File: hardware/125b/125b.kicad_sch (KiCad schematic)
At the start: 56 parts, among them J1 Guitar in, J2 fsw pin 1, J3 fsw pin 2, J4 fsw pin 4, J5 fsw pin 5, J6 fsw pin 6, J7 Left out, J8 Right out, J9 fsw pin 3, SW1 Switch 1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

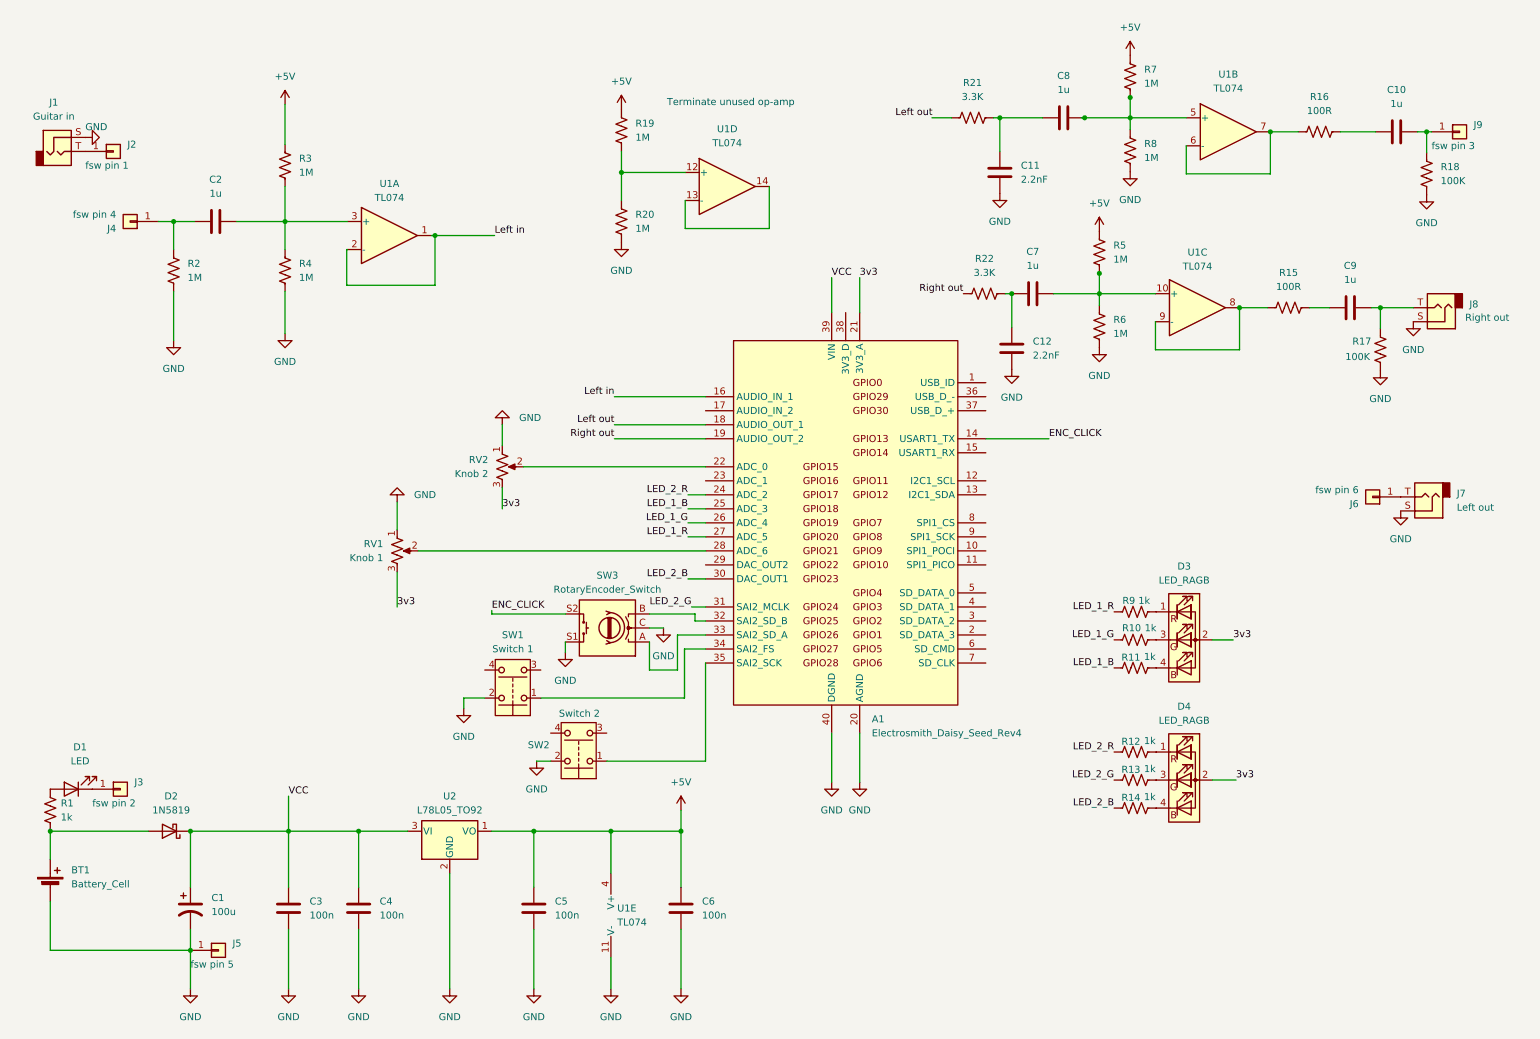
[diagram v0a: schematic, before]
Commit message: Add switch for line input toggle and fix stereo out
Bypass will be different for stereo out
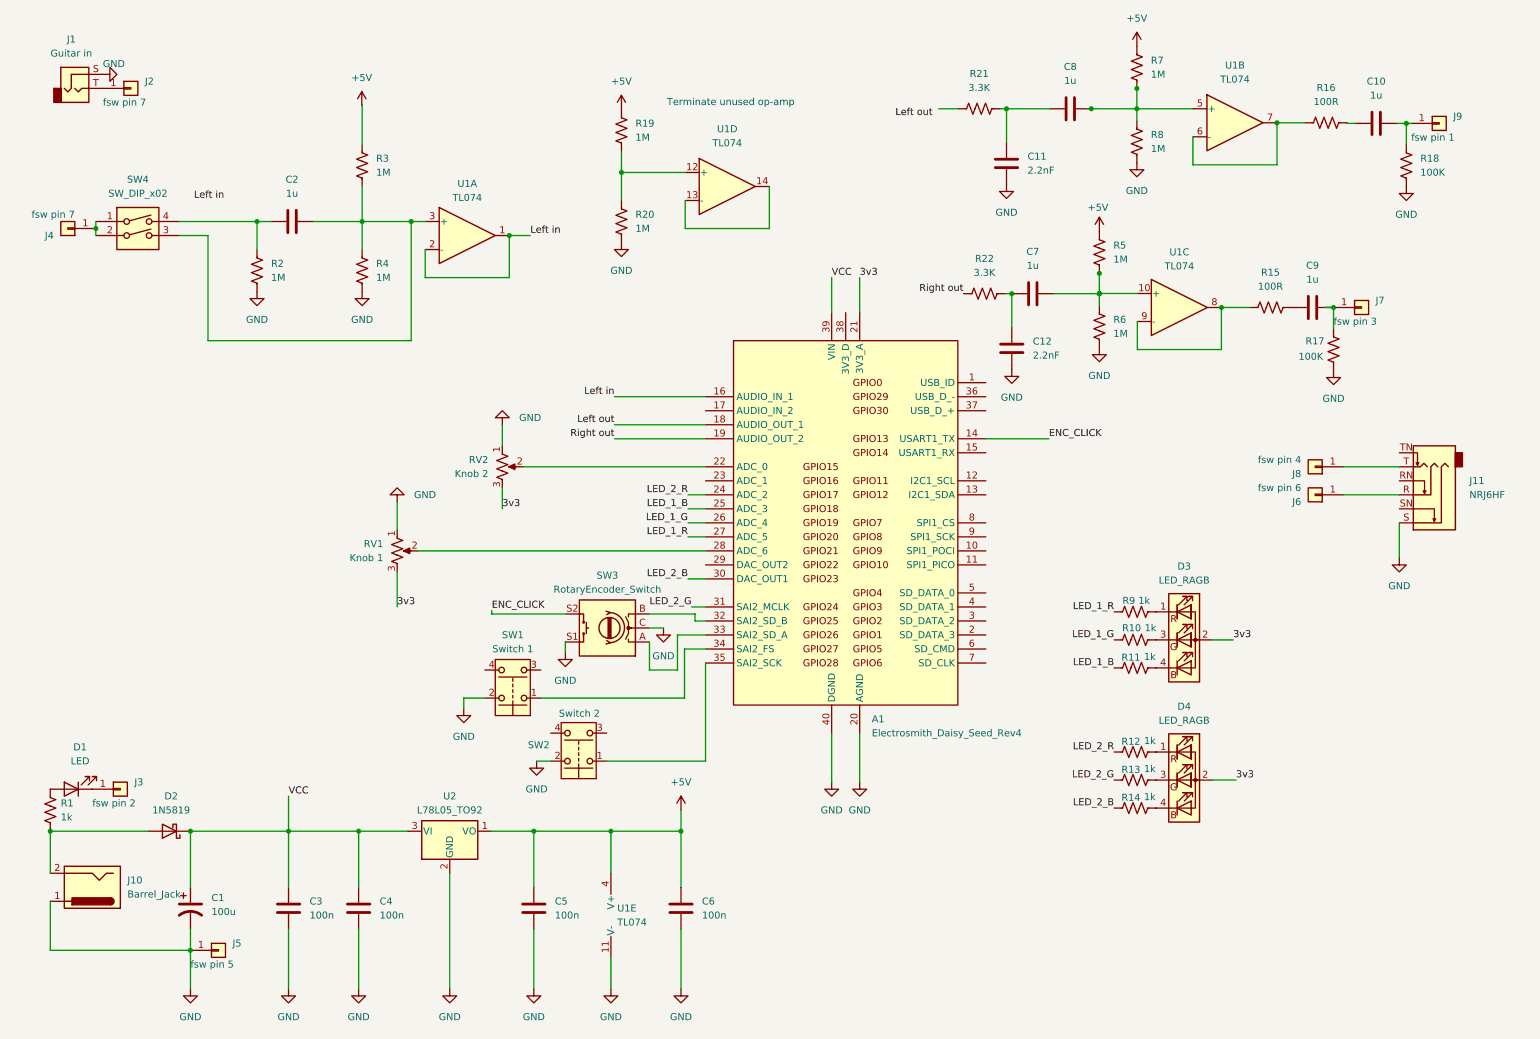
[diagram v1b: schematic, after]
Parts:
- removed BT1: Battery_Cell, Connector_Wire:SolderWire-0.25sqmm_1x02_P4.2mm_D0.65mm_OD1.7mm, symbol Device:Battery_Cell
- removed J7: Left out, Connector_Wire:SolderWire-0.25sqmm_1x01_D0.65mm_OD2mm, symbol Connector_Audio:AudioJack2
- removed J8: Right out, Connector_Wire:SolderWire-0.25sqmm_1x01_D0.65mm_OD2mm, symbol Connector_Audio:AudioJack2
- added J10: Barrel_Jack, symbol Connector:Barrel_Jack
- added J11: NRJ6HF, Connector_Audio:Jack_6.35mm_Neutrik_NRJ6HF_Horizontal, symbol Connector_Audio:NRJ6HF
- added J7: fsw pin 3, Connector_Wire:SolderWire-0.25sqmm_1x01_D0.65mm_OD2mm, symbol Connector_Generic:Conn_01x01
- added J8: fsw pin 4, Connector_Wire:SolderWire-0.25sqmm_1x01_D0.65mm_OD2mm, symbol Connector_Generic:Conn_01x01
- added SW4: SW_DIP_x02, symbol Switch:SW_DIP_x02
- J2: value fsw pin 1 -> fsw pin 7
- J4: value fsw pin 4 -> fsw pin 7
- J9: value fsw pin 3 -> fsw pin 1
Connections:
- net +5V: no longer R3.1
- net GND: now also J10.1, J11.S
- net Left out: no longer R21.1
- net at R3.2, R4.1: now also SW4.3; no longer C2.2, U1.3 (+)
- net at C9.2, R17.1: now also J7.1 (Pin_1)
- net at D2.2 (A), R1.1: now also J10.2
- net at C2.1, R2.1: now also SW4.4; no longer J4.1 (Pin_1)
- net at J6.1 (Pin_1): now also J11.R
- new net: J11.T, J8.1 (Pin_1)
- new net: J4.1 (Pin_1), SW4.1, SW4.2
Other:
- title: DaisyPdal -> Podal
- moved on the sheet: C10, C11, C2, C8, C9, J1, J2, J4, J6, J9, R15, R16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

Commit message: Tidy up scehmatic - grid snapping
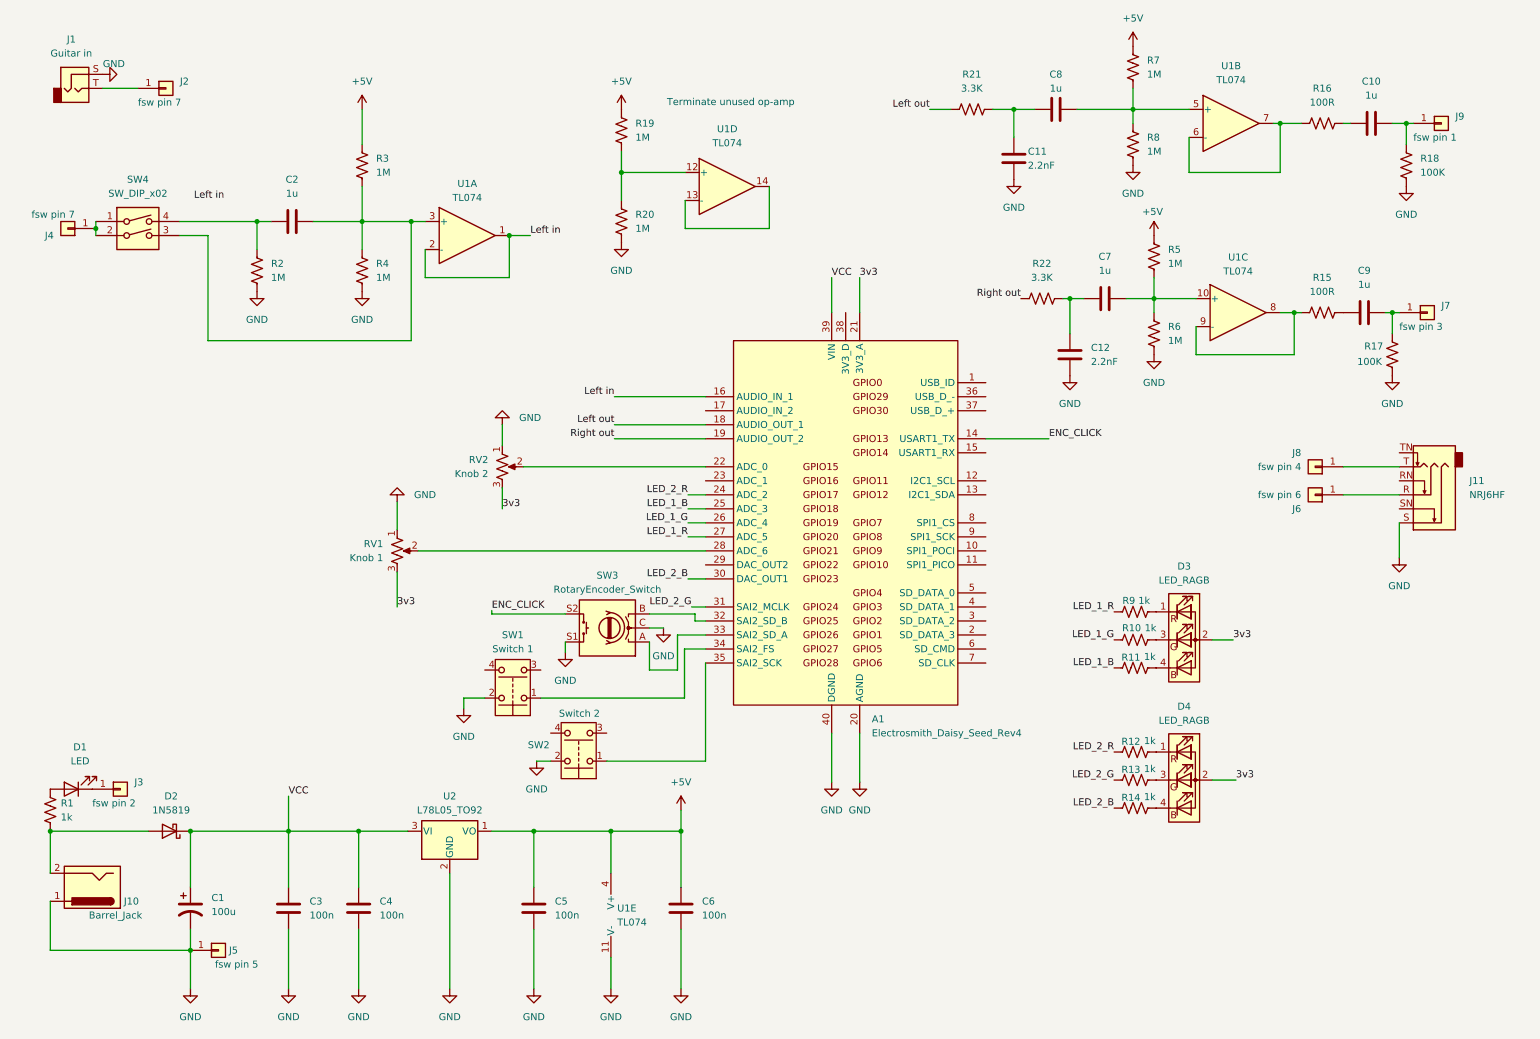
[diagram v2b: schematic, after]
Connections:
- net +5V: now also R3.1
- net Left out: now also R21.1
- net at R3.2, R4.1, SW4.3: now also C2.2, U1.3 (+)
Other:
- moved on the sheet: C10, C11, C12, C7, C8, C9, J2, J7, R15, R16, R17, R21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

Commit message: Update PCB and resize for 125b
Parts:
- J10: footprint (none) -> Connector_BarrelJack:BarrelJack_Horizontal
- SW4: footprint (none) -> Button_Switch_SMD:SW_DIP_SPSTx02_Slide_9.78x7.26mm_W8.61mm_P2.54mm
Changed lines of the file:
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@@
 			)
 		)
-		(property "Footprint" ""
+		(property "Footprint" "Connector_BarrelJack:BarrelJack_Horizontal"
 			(at 24.765 170.434 0)
 			(effects
@@
 			)
 		)
-		(property "Footprint" ""
+		(property "Footprint" "Button_Switch_SMD:SW_DIP_SPSTx02_Slide_9.78x7.26mm_W8.61mm_P2.54mm"
 			(at 34.29 53.34 0)
 			(effects

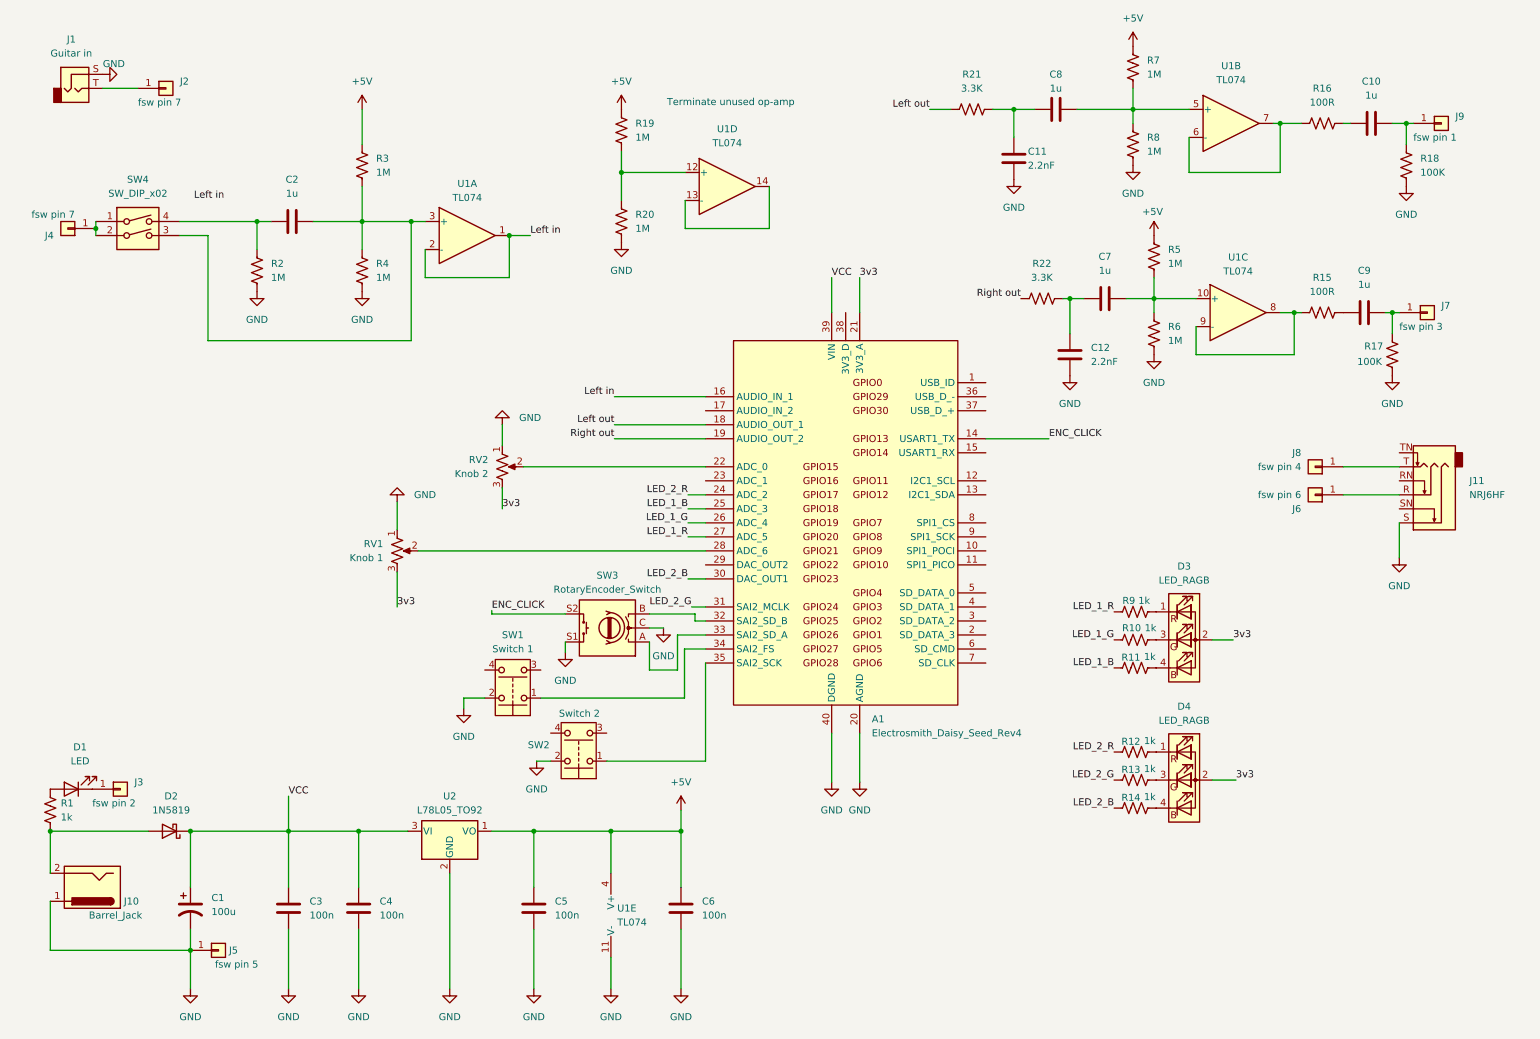
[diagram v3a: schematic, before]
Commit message: Tidy up schematic
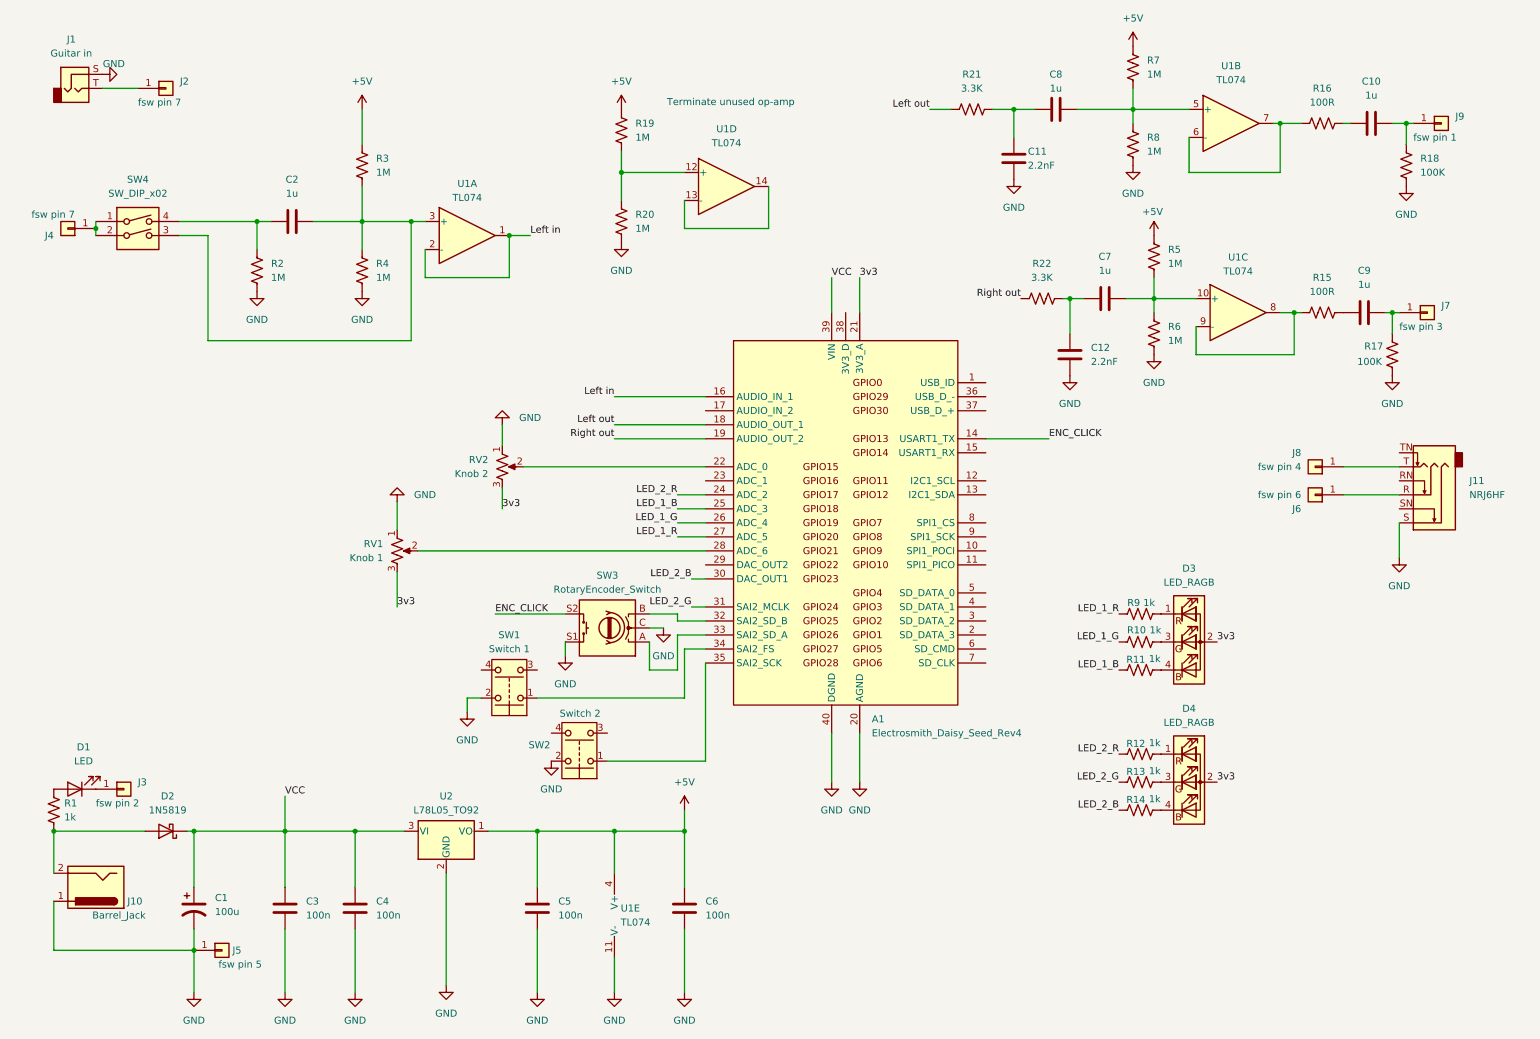
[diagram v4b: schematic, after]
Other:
- moved on the sheet: C1, C3, C4, C5, C6, D1, D2, D3, D4, J10, J3, J5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

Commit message: Footprints for audio and power sockets added
Also DIP switch for line/ guitar input. Ready to start
moving components around.
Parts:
- J1: footprint Connector_Wire:SolderWire-0.25sqmm_1x01_D0.65mm_OD2mm -> Connector_Audio:Jack_6.35mm_Neutrik_NRJ6HF-1-AU_Horizontal
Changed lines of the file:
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@@
 			)
 		)
-		(property "Footprint" "Connector_Wire:SolderWire-0.25sqmm_1x01_D0.65mm_OD2mm"
+		(property "Footprint" "Connector_Audio:Jack_6.35mm_Neutrik_NRJ6HF-1-AU_Horizontal"
 			(at 22.86 26.67 0)
 			(effects
